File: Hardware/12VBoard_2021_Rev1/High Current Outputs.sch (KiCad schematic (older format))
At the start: 15 parts, among them U6 LM2576S-12/NOPB

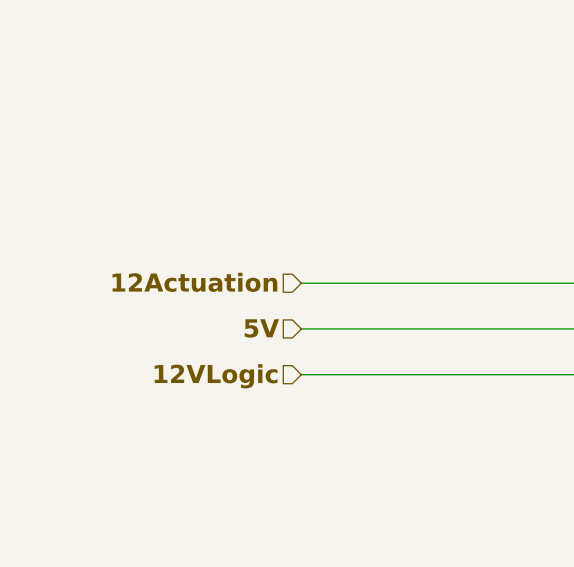
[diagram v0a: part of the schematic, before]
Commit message: fixed 12VAcutation issue
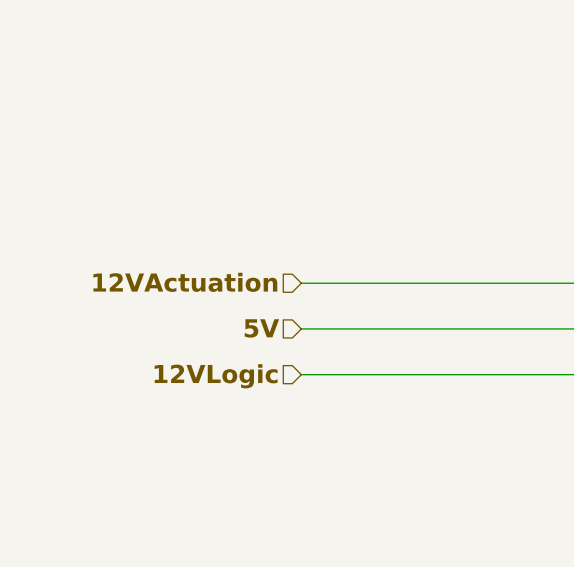
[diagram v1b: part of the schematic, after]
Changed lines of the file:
@@
 Connection ~ 3325 6850
 Text HLabel 1825 5275 0    79   Input ~ 16
-12Actuation
+12VActuation
 Wire Wire Line
 	1825 5275 3750 5275

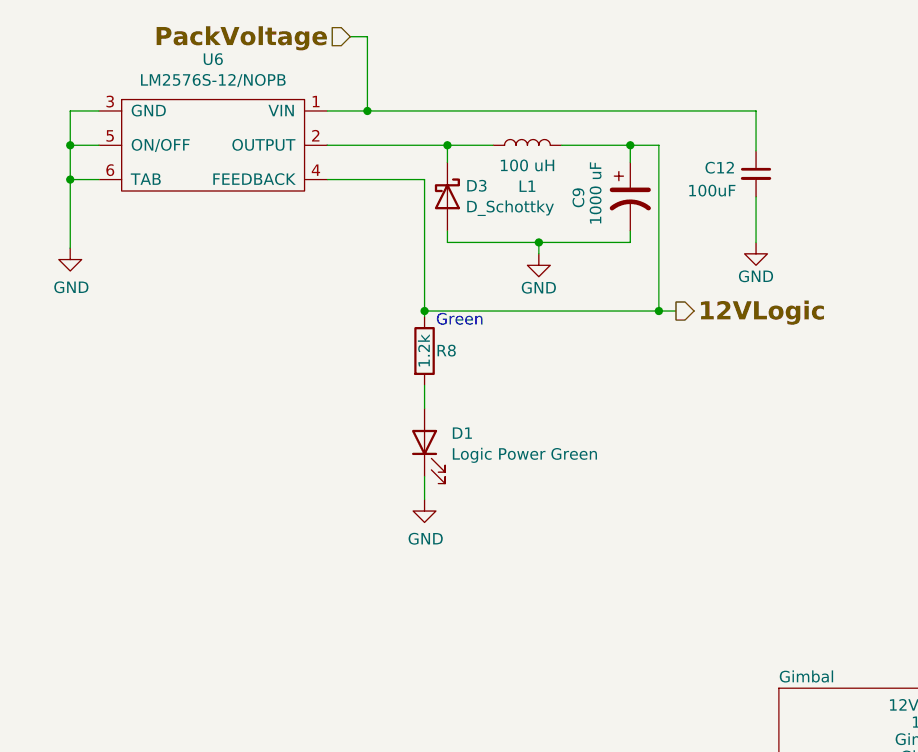
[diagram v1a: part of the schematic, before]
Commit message: admin changes
-current sensing on high current
-fixed traces for current sensing
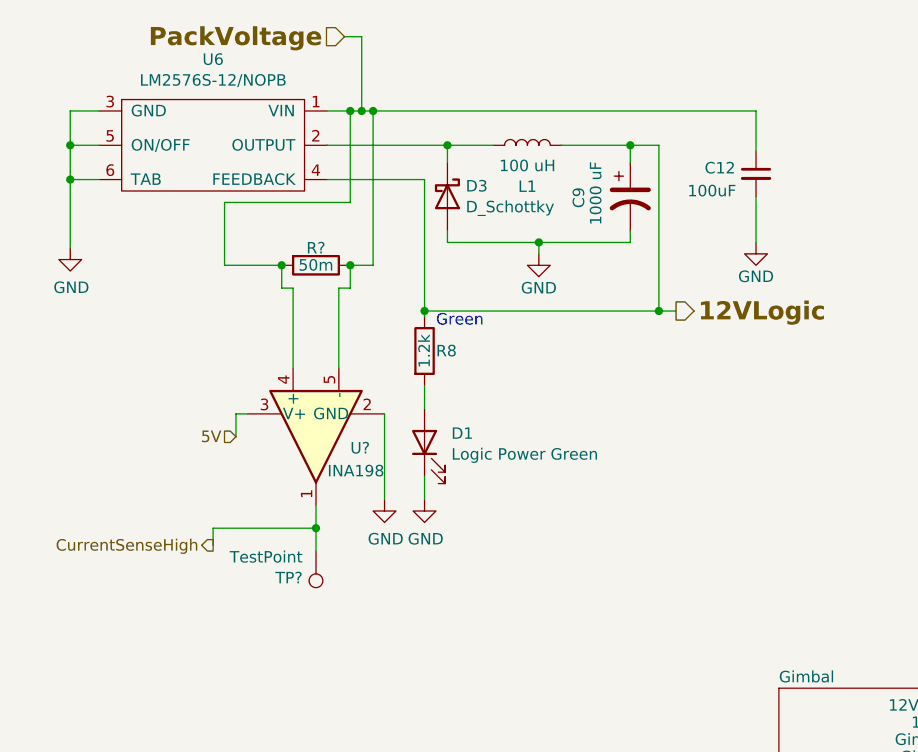
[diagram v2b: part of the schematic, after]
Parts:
- added R?: 50m, Package_TO_SOT_THT:TO-126-2_Vertical, symbol Device:R
- added TP?: TestPoint, TestPoint:TestPoint_Pad_2.5x2.5mm, symbol Connector:TestPoint
- added U?: INA198, Package_TO_SOT_SMD:SOT-23-5, symbol Amplifier_Current:INA198
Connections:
- net 5V: now also U?.3 (V+)
- net GND: now also U?.2 (GND)
- net PackVoltage: now also R?.1, R?.2, U?.4 (+), U?.5 (-)
- new net CurrentSenseHigh: TP?.1, U?.1
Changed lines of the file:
@@
 EESchema Schematic File Version 4
+LIBS:12VBoard_2021_Rev1-cache
 EELAYER 30 0
 EELAYER END
@@
 Wire Wire Line
 	3150 6850 3150 6900
-$Comp
-L Device:CP1_Small C10
-U 1 1 6056D755
-P 3325 6975
-F 0 "C10" H 3350 7050 50  0000 L CNN
-F 1 "330uF" H 3350 6875 50  0000 L CNN
-F 2 "Capacitor_THT:CP_Radial_D8.0mm_P3.50mm" H 3325 6975 50  0001 C CNN
-F 3 "~" H 3325 6975 50  0001 C CNN
-	1    3325 6975
-	1    0    0    -1
-$EndComp
 Wire Wire Line
 	3150 6850 3325 6850
@@
 Text HLabel 1825 5675 0    79   Input ~ 16
 12VLogic
-Wire Wire Line
-	1825 5675 3600 5675
 Wire Wire Line
 	725  1150 725  1300
@@
 $EndComp
 Wire Wire Line
-	1950 675  2025 675
-Text HLabel 1950 675  0    79   Input ~ 16
+	1925 675  2000 675
+Text HLabel 1925 675  0    79   Input ~ 16
 PackVoltage
 $Comp
@@
 	3725 1000 3725 1175
 Wire Wire Line
-	1850 1000 2025 1000
+	1850 1000 1950 1000
 Wire Wire Line
 	1850 1150 2375 1150
@@
 	2275 1300 2275 1875
 Wire Wire Line
-	2025 675  2025 1000
-Connection ~ 2025 1000
-Wire Wire Line
-	2025 1000 3725 1000
+	2000 675  2000 1000
 Wire Wire Line
 	3300 1150 3300 1875
@@
 Wire Wire Line
 	2275 1875 3300 1875
+Wire Wire Line
+	1825 5675 3600 5675
+Connection ~ 1650 1675
+Wire Wire Line
+	1650 1675 1400 1675
+Connection ~ 1950 1675
+Wire Wire Line
+	1950 1675 2050 1675
+Wire Wire Line
+	1800 2825 1350 2825
+Wire Wire Line
+	1350 2825 1350 2900
+Connection ~ 1800 2825
+Wire Wire Line
+	1800 2825 1800 2925
+$Comp
+L Connector:TestPoint TP?
+U 1 1 5FCE5BE7
+P 1800 2925
+AR Path="/5F74F223/5FCE5BE7" Ref="TP?"  Part="1"
+AR Path="/5F74F36B/5FCE5BE7" Ref="TP?"  Part="1"
+F 0 "TP?" H 1858 3043 50  0000 L CNN
+F 1 "TestPoint" H 1858 2952 50  0000 L CNN
+F 2 "TestPoint:TestPoint_Pad_2.5x2.5mm" H 2000 2925 50  0001 C CNN
+F 3 "~" H 2000 2925 50  0001 C CNN
+	1    1800 2925
+	-1   0    0    1
+$EndComp
+Wire Wire Line
+	1800 2825 1800 2725
+Text HLabel 1350 2900 0    50   Output ~ 0
+CurrentSenseHigh
+Wire Wire Line
+	1450 2325 1450 2425
+Wire Wire Line
+	1500 2325 1450 2325
+Text HLabel 1450 2425 0    50   Input ~ 0
+5V
+$Comp
+L Amplifier_Current:INA198 U?
+U 1 1 5FCE5BF3
+P 1800 2425
+AR Path="/5F74F36B/5F8236F9/5FCE5BF3" Ref="U?"  Part="1"
+AR Path="/5F74F223/5FCE5BF3" Ref="U?"  Part="1"
+AR Path="/5F74F36B/5FCE5BF3" Ref="U?"  Part="1"
+F 0 "U?" V 1850 2275 50  0000 R CNN
+F 1 "INA198" V 1950 2375 50  0000 R CNN
+F 2 "Package_TO_SOT_SMD:SOT-23-5" H 1800 2425 50  0001 C CNN
+F 3 "http://www.ti.com/lit/ds/symlink/ina193.pdf" H 1800 2425 50  0001 C CNN
+	1    1800 2425
+	0    -1   1    0
+$EndComp
+$Comp
+L Device:R R?
+U 1 1 5FCE5BF9
+P 1800 1675
+AR Path="/5F74F36B/5F8236F9/5FCE5BF9" Ref="R?"  Part="1"
+AR Path="/5F74F223/5FCE5BF9" Ref="R?"  Part="1"
+AR Path="/5F74F36B/5FCE5BF9" Ref="R?"  Part="1"
+F 0 "R?" V 1725 1675 50  0000 C CNN
+F 1 "50m" V 1800 1675 50  0000 C CNN
+F 2 "Package_TO_SOT_THT:TO-126-2_Vertical" V 1730 1675 50  0001 C CNN
+F 3 "~" H 1800 1675 50  0001 C CNN
+	1    1800 1675
+	0    1    1    0
+$EndComp
+Wire Wire Line
+	1700 2125 1700 1775
+Wire Wire Line
+	1700 1775 1650 1775
+Wire Wire Line
+	1650 1775 1650 1675
+Wire Wire Line
+	1900 2125 1900 1775
+Wire Wire Line
+	1900 1775 1950 1775
+Wire Wire Line
+	1950 1775 1950 1675
+$Comp
+L power:GND #PWR?
+U 1 1 5FD0A1AA
+P 2100 2700
+F 0 "#PWR?" H 2100 2450 50  0001 C CNN
+F 1 "GND" H 2105 2527 50  0000 C CNN
+F 2 "" H 2100 2700 50  0001 C CNN
+F 3 "" H 2100 2700 50  0001 C CNN
+	1    2100 2700
+	1    0    0    -1
+$EndComp
+Wire Wire Line
+	2100 2700 2100 2325
+Wire Wire Line
+	2050 1000 2050 1675
+Connection ~ 2050 1000
+Wire Wire Line
+	2050 1000 3725 1000
+Wire Wire Line
+	1400 1400 1950 1400
+Wire Wire Line
+	1950 1400 1950 1000
+Wire Wire Line
+	1400 1400 1400 1675
+Connection ~ 1950 1000
+Wire Wire Line
+	1950 1000 2000 1000
+Connection ~ 2000 1000
+Wire Wire Line
+	2000 1000 2050 1000
+$Comp
+L Device:CP1_Small C10
+U 1 1 6056D755
+P 3325 6975
+F 0 "C10" H 3350 7050 50  0000 L CNN
+F 1 "330uF" H 3350 6875 50  0000 L CNN
+F 2 "Capacitor_THT:CP_Radial_D8.0mm_P3.50mm" H 3325 6975 50  0001 C CNN
+F 3 "~" H 3325 6975 50  0001 C CNN
+	1    3325 6975
+	1    0    0    -1
+$EndComp
 $EndSCHEMATC

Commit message: Started work on BOM
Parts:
- R24: renamed from R?; footprint Package_TO_SOT_THT:TO-126-2_Vertical -> Resistor_SMD:R_1206_3216Metric_Pad1.42x1.75mm_HandSolder
- gave numbers to parts that had none: 2
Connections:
- net PackVoltage: no longer C12.1, R24.2, U21.4 (+), U6.1 (VIN)
- new net: C12.1, R24.2, U21.4 (+), U6.1 (VIN)
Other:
- moved on the sheet: C12, C9, D1, D3, L1, R24, R8, TP2, U21, U6

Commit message: Discovered problems, will fix on next pushes
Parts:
- R24: value 50m -> 20m
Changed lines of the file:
@@
 AR Path="/5F74F36B/5FCE5BF9" Ref="R24"  Part="1"
 F 0 "R24" V 2395 1730 50  0000 C CNN
-F 1 "50m" V 2470 1730 50  0000 C CNN
+F 1 "20m" V 2470 1730 50  0000 C CNN
 F 2 "Resistor_SMD:R_1206_3216Metric_Pad1.42x1.75mm_HandSolder" V 2400 1730 50  0001 C CNN
 F 3 "~" H 2470 1730 50  0001 C CNN

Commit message: Fixed problem
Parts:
- removed C11: 330uF, Capacitor_THT:CP_Radial_D8.0mm_P3.50mm, symbol Device:CP1_Small
- removed C12: 100uF, Capacitor_SMD:C_0603_1608Metric_Pad1.05x0.95mm_HandSolder, symbol Device:C_Small
- removed C9: 1000 uF, Capacitor_THT:CP_Radial_D10.0mm_P5.00mm, symbol Device:CP1
- removed D1: Logic Power Green, Diode_SMD:D_0603_1608Metric_Pad1.05x0.95mm_HandSolder, symbol Device:LED
- removed D3: D_Schottky, Diode_THT:D_DO-201AD_P5.08mm_Vertical_KathodeUp, symbol Device:D_Schottky
- removed F2: 20, MRDT_Passives:ATC_Fuse_Block, symbol Device:Fuse_Small
- removed L1: 100 uH, Inductor_SMD:L_0603_1608Metric_Pad1.05x0.95mm_HandSolder, symbol Device:L
- removed R24: 20m, Resistor_SMD:R_1206_3216Metric_Pad1.42x1.75mm_HandSolder, symbol Device:R
- removed R8: 1.2k, Resistor_SMD:R_0603_1608Metric_Pad1.05x0.95mm_HandSolder, symbol Device:R
- removed TP2: TestPoint, TestPoint:TestPoint_Pad_2.5x2.5mm, symbol Connector:TestPoint
- removed U21: INA198, Package_TO_SOT_SMD:SOT-23-5, symbol Amplifier_Current:INA198
- removed U6: LM2576S-12/NOPB, MRDT_Devices:LM2576, symbol 12VBoard_2021_Rev1-rescue:LM2576D2TR4-MRDT_Devices
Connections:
- net 12VActuation: now also C10.1, VR1.7 (SENSE(+)), VR1.8 (+VOUT)
- net GND: no longer VR1.2 (REMOTE)
- new net BuckCTL: VR1.2 (REMOTE)
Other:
- note removed: "Green"

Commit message: Started Rev 2
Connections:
- net BuckCTL is gone; now on net GND: VR1.2 (REMOTE)
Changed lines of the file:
@@
 Wire Wire Line
 	1850 7150 1750 7150
-Wire Wire Line
-	1850 7000 1750 7000
 NoConn ~ 3000 7000
 Wire Wire Line
@@
 Wire Wire Line
 	3325 6850 4050 6850
-Text HLabel 1750 7000 0    79   Input ~ 16
-BuckCTL
+Wire Wire Line
+	1850 7000 1750 7000
+Wire Wire Line
+	1750 7000 1750 7150
+Connection ~ 1750 7150
 $EndSCHEMATC

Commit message: Rev 2 redone
in conclusion rev2=rev3 but its really rev12
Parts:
- removed Conn10: AuxMount, MRDT_Connectors:Anderson_3_Vertical_Side_by_Side, symbol MRDT_Connectors:AndersonPP
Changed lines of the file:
@@
 $Descr A4 11693 8268
 encoding utf-8
-Sheet 5 8
+Sheet 5 7
 Title ""
 Date ""
@@
 Comment4 ""
 $EndDescr
-$Comp
-L MRDT_Connectors:AndersonPP Conn?
-U 1 1 5F9C014B
-P 7925 2375
-AR Path="/5F74F36B/5F821EB2/5F9C014B" Ref="Conn?"  Part="1"
-AR Path="/5F74F36B/5F9C014B" Ref="Conn10"  Part="1"
-F 0 "Conn10" H 7897 2422 60  0000 R CNN
-F 1 "AuxMount" H 7897 2528 60  0000 R CNN
-F 2 "MRDT_Connectors:Anderson_3_Vertical_Side_by_Side" H 7775 1825 60  0001 C CNN
-F 3 "" H 7775 1825 60  0001 C CNN
-	1    7925 2375
-	-1   0    0    1
-$EndComp
-$Comp
-L MRDT_Connectors:AndersonPP Conn?
-U 3 1 5F9C0151
-P 7925 2125
-AR Path="/5F74F36B/5F821EB2/5F9C0151" Ref="Conn?"  Part="2"
-AR Path="/5F74F36B/5F9C0151" Ref="Conn10"  Part="3"
-F 0 "Conn10" H 7897 2172 60  0000 R CNN
-F 1 "AuxMount" H 7897 2278 60  0000 R CNN
-F 2 "MRDT_Connectors:Anderson_3_Vertical_Side_by_Side" H 7775 1575 60  0001 C CNN
-F 3 "" H 7775 1575 60  0001 C CNN
-	3    7925 2125
-	-1   0    0    1
-$EndComp
-$Comp
-L power:GND #PWR?
-U 1 1 5F9C0157
-P 7475 2525
-AR Path="/5F74F36B/5F821EB2/5F9C0157" Ref="#PWR?"  Part="1"
-AR Path="/5F74F36B/5F9C0157" Ref="#PWR033"  Part="1"
-F 0 "#PWR033" H 7475 2275 50  0001 C CNN
-F 1 "GND" H 7480 2352 50  0000 C CNN
-F 2 "" H 7475 2525 50  0001 C CNN
-F 3 "" H 7475 2525 50  0001 C CNN
-	1    7475 2525
-	1    0    0    -1
-$EndComp
-Wire Wire Line
-	7525 2475 7475 2475
-Wire Wire Line
-	7475 2475 7475 2525
-Wire Wire Line
-	7275 3675 7375 3675
-Wire Wire Line
-	7375 3675 7375 2225
-Wire Wire Line
-	7375 2225 7525 2225
 $Comp
 L MRDT_Connectors:AndersonPP Conn?
@@
 	9400 3625 9475 3625
 Wire Wire Line
-	7275 3600 7350 3600
-Wire Wire Line
-	7350 3600 7350 1975
-Wire Wire Line
 	4925 3600 5000 3600
 Wire Wire Line
@@
 	5000 1975 5175 1975
 $Comp
-L MRDT_Connectors:AndersonPP Conn10
-U 2 1 5FB53487
-P 7925 1875
-F 0 "Conn10" H 7897 1922 60  0000 R CNN
-F 1 "AuxMount" H 7897 2028 60  0000 R CNN
-F 2 "MRDT_Connectors:Anderson_3_Vertical_Side_by_Side" H 7775 1325 60  0001 C CNN
-F 3 "" H 7775 1325 60  0001 C CNN
-	2    7925 1875
-	-1   0    0    1
-$EndComp
-Wire Wire Line
-	7350 1975 7525 1975
-$Comp
 L MRDT_Connectors:AndersonPP Conn11
 U 2 1 5FB56BDF
@@
 Wire Wire Line
 	9475 2000 9475 2950
-$Sheet
-S 6025 3525 1250 1450
-U 5F8222BE
-F0 "AuxMount" 50
-F1 "AuxMount.sch" 50
-F2 "12V10AAuxMount" O R 7275 3675 50
-F3 "AuxMountCTL_Act" I R 7275 3825 50
-F4 "AuxMountSense" O R 7275 3900 50
-F5 "5V" I L 6025 4800 49
-F6 "12VLogicAuxMount" O R 7275 3600 50
-F7 "12VActuation" I L 6025 4875 50
-F8 "AuxMountCTL_Log" I R 7275 3750 50
-F9 "12VLogic" I L 6025 4710 50
-$EndSheet
 $Sheet
 S 3825 3525 1100 1450
@@
 	8000 4825 8150 4825
 Wire Wire Line
-	6025 4875 5925 4875
-Wire Wire Line
-	5925 4875 5925 5275
-Wire Wire Line
-	6025 4800 5850 4800
-Wire Wire Line
-	5850 4800 5850 5475
-Connection ~ 5850 5475
-Wire Wire Line
-	5850 5475 8000 5475
-Wire Wire Line
 	1825 5475 3675 5475
 Wire Wire Line
@@
 	3675 4800 3675 5475
 Connection ~ 3675 5475
-Wire Wire Line
-	3675 5475 5850 5475
 Wire Wire Line
 	9500 3200 9750 3200
@@
 Text HLabel 5125 3900 2    50   Output ~ 0
 GimbalSense
-Text HLabel 7425 3750 2    50   Input ~ 0
-AuxMountCTL_Log
-Text HLabel 7425 3825 2    50   Input ~ 0
-AuxMountCTL_Act
-Text HLabel 7425 3900 2    50   Output ~ 0
-AuxMountSense
 Text HLabel 9575 3850 2    50   Input ~ 0
 MultimediaCTL_Act
@@
 Wire Wire Line
 	9400 3850 9575 3850
-Wire Wire Line
-	7275 3750 7425 3750
-Wire Wire Line
-	7275 3825 7425 3825
-Wire Wire Line
-	7275 3900 7425 3900
 Wire Wire Line
 	4925 3750 5125 3750
@@
 Wire Wire Line
 	1825 5275 3750 5275
-Wire Wire Line
-	3750 5275 5925 5275
 Connection ~ 3750 5275
-Wire Wire Line
-	5925 5275 8075 5275
-Connection ~ 5925 5275
 $Comp
 L Device:CP1_Small C10
@@
 Wire Wire Line
 	3570 4700 3825 4700
-Wire Wire Line
-	3570 5620 5730 5620
-Wire Wire Line
-	5730 5620 5730 4710
-Wire Wire Line
-	5730 4710 6025 4710
 Connection ~ 3570 5620
 Wire Wire Line
-	5730 5620 7935 5620
-Wire Wire Line
 	7935 5620 7935 4755
 Wire Wire Line
 	7935 4755 8150 4755
-Connection ~ 5730 5620
 Wire Wire Line
 	3325 6850 4050 6850
@@
 	1750 7000 1750 7150
 Connection ~ 1750 7150
+Wire Wire Line
+	3750 5275 8075 5275
+Wire Wire Line
+	3675 5475 8000 5475
+Wire Wire Line
+	3570 5620 7935 5620
 $EndSCHEMATC
